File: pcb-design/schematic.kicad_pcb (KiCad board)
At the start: 2 copper layers, 130.8 x 139.7 mm, 74 parts, among them J4 Screw_Terminal_01x02, J6 Conn_02x13_Top_Bottom, Q1 2N2222, Q2 2N2222, Q3 2N2222, Q6 2N2222, Q8 2N3906, U2 MCP23017_SP, U3 MCP2562-E-P, U4 AP1117-33, U6 ESP32-DEVKITC-32D, U7 L7805

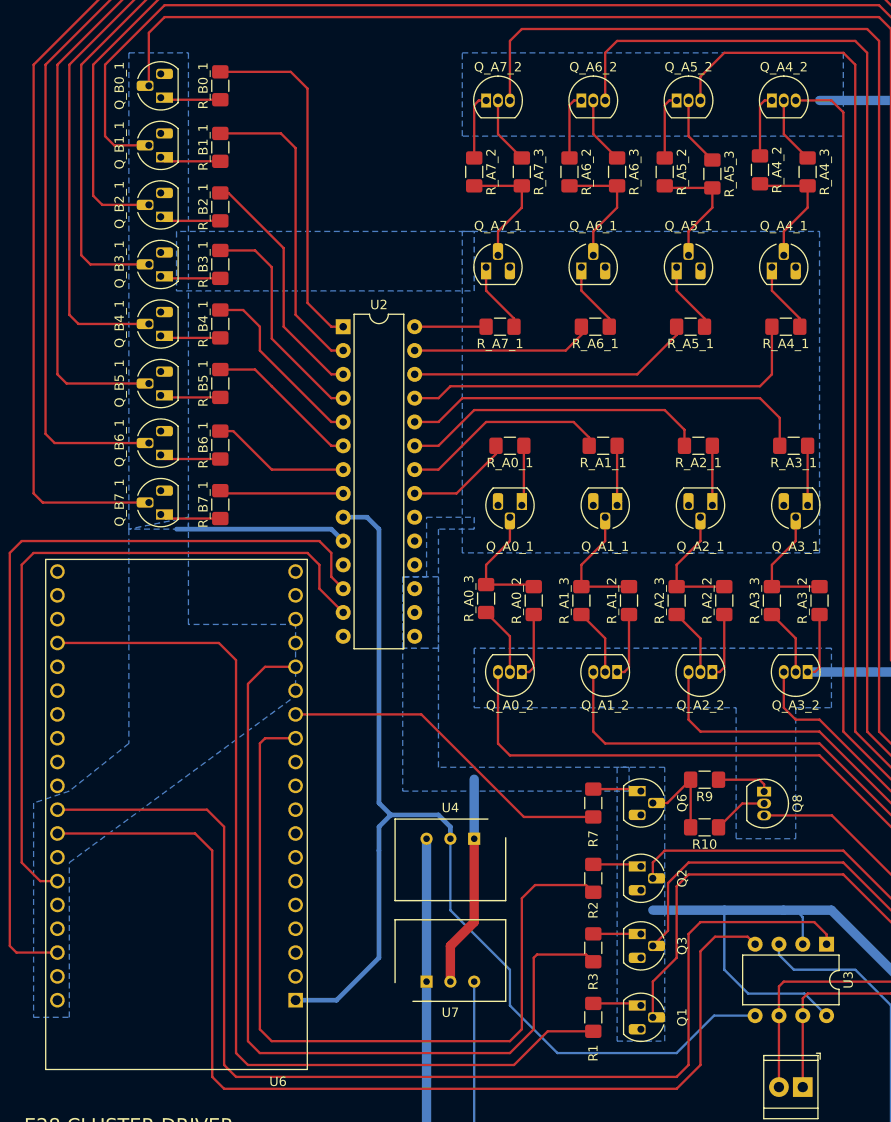
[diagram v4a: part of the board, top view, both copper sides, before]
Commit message: Updated resistor footprints to 0805 which had better coverage for JLCPCB basic parts.
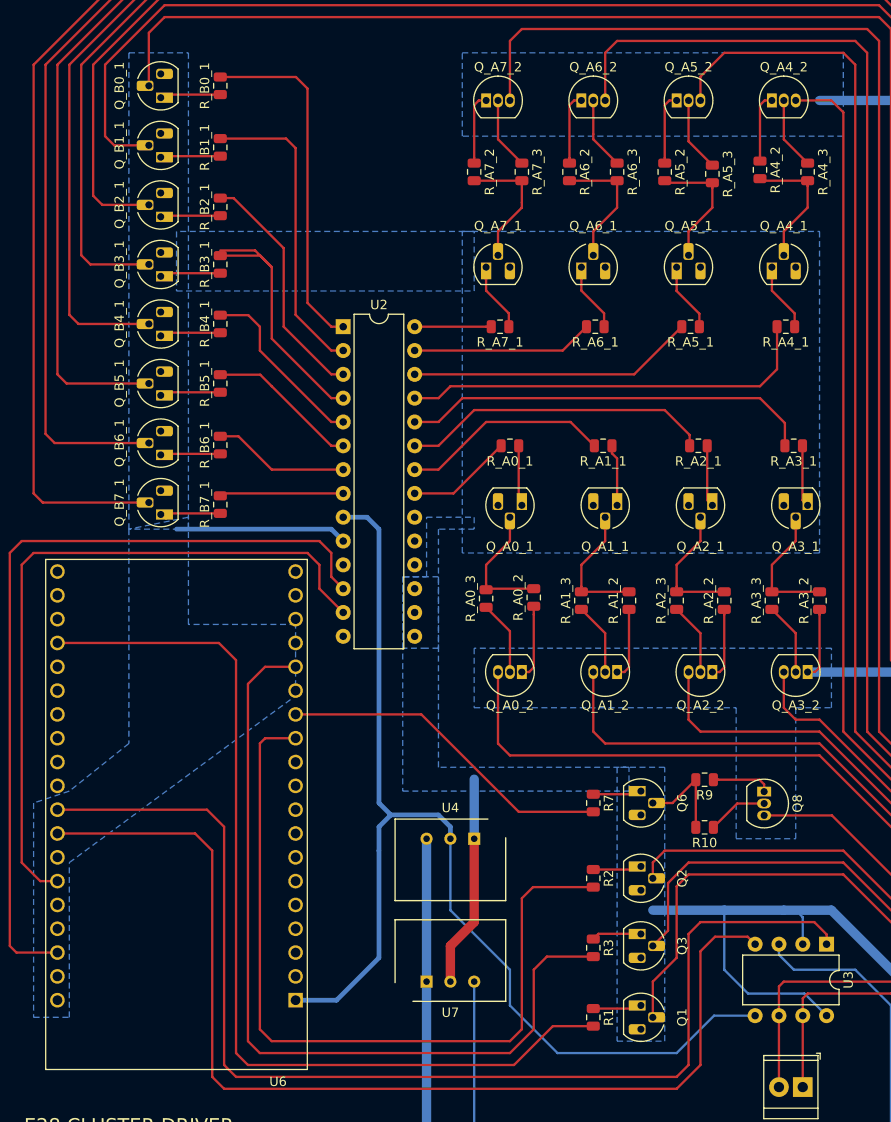
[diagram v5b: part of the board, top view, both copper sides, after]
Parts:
- R1, R2, R3, R9, R_A0_2, R_A1_2, R_A2_2, R_A3_2, R_A4_2, R_A5_2, R_A6_2, R_A7_2: footprint Resistor_SMD:R_1206_3216Metric_Pad1.42x1.75mm_HandSolder -> Resistor_SMD:R_0805_2012Metric
- R10, R7, R_A0_1, R_A0_3, R_A1_1, R_A1_3, R_A2_1, R_A2_3, R_A3_1, R_A3_3, R_A4_1, R_A4_3, R_A5_1, R_A5_3, R_A6_1, R_A6_3, R_A7_1, R_A7_3, R_B0_1, R_B1_1, R_B2_1, R_B3_1, R_B4_1, R_B5_1, R_B6_1, R_B7_1: value 4000 -> 4700; footprint Resistor_SMD:R_1206_3216Metric_Pad1.42x1.75mm_HandSolder -> Resistor_SMD:R_0805_2012Metric
- U6: footprint MODULE_ESP32-DEVKITC-32D -> pcb-design:MODULE_ESP32-DEVKITC-32D
- moved R_A0_2 0.33 mm to (108.0, 106.3)
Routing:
- net Net-(R_B3_1-Pad2): track 24.1 -> 30.1 mm
- net +12V: track 324.9 -> 330.1 mm
- net SpeedometerSignal: track 90.4 -> 89.3 mm
- net Net-(Q_B7_1-Pad1): track 6.53 -> 7.13 mm
- net Net-(Q_A3_1-Pad2): track 13.5 -> 14.1 mm
- net Net-(Q_A2_1-Pad2): track 13.5 -> 14.1 mm
- net Net-(Q_A1_1-Pad2): track 13.5 -> 14.1 mm
- net Net-(Q_A7_2-Pad2): track 7.18 -> 7.73 mm
- net Net-(Q_A6_2-Pad2): track 7.18 -> 7.73 mm
- net Net-(Q_A5_2-Pad2): track 7.40 -> 7.95 mm
- net Net-(Q_A4_2-Pad2): track 7.18 -> 7.73 mm
- net Net-(R_A7_1-Pad2): track 7.62 -> 8.17 mm
- net Net-(Q_A7_1-Pad2): track 13.5 -> 14.1 mm
- net Net-(Q_A6_1-Pad2): track 13.5 -> 14.1 mm
- net Net-(Q_A3_2-Pad2): track 7.18 -> 7.73 mm
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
